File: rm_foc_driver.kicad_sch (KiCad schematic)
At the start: 88 parts, among them J1 SWD, J2 TMC4671, J3 UART, J4 TMC4671, J5 Conn_01x03, J6 Conn_01x02, J8 Conn_01x03, Q1 CSD18540Q5B, Q2 CSD18540Q5B, Q3 CSD18540Q5B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

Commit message: version 1.0.0-beta
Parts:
- removed C11, C9: 22pF, Capacitor_SMD:C_0603_1608Metric, symbol Device:C
- removed C34, C35, C36, C37: 100nF, Capacitor_SMD:C_0603_1608Metric, symbol Device:C
- removed C6: 4.7uF, Capacitor_SMD:C_0603_1608Metric, symbol Device:C
- removed D1, D2: LED, LED_SMD:LED_0603_1608Metric, symbol Device:LED
- removed J3: UART, Connector_PinHeader_2.54mm:PinHeader_1x04_P2.54mm_Horizontal, symbol Connector_Generic:Conn_01x04
- removed J4: TMC4671, Connector_PinHeader_2.54mm:PinHeader_1x04_P2.54mm_Vertical, symbol Connector_Generic:Conn_01x04
- removed J5: Conn_01x03, Connector_PinSocket_2.54mm:PinSocket_1x03_P2.54mm_Vertical, symbol Connector_Generic:Conn_01x03
- removed U3: STM32F401CCUx, Package_DFN_QFN:QFN-48-1EP_7x7mm_P0.5mm_EP5.6x5.6mm, symbol MCU_ST_STM32F4:STM32F401CCUx
- removed Y1: Crystal_GND24, Crystal:Crystal_SMD_3225-4Pin_3.2x2.5mm, symbol Device:Crystal_GND24
- added J3: Conn_01x03, Connector_PinHeader_2.54mm:PinHeader_1x03_P2.54mm_Vertical, symbol Connector_Generic:Conn_01x03
- added R21, R22: 10k, Resistor_SMD:R_0603_1608Metric, symbol Device:R
- added U3: ADS1115IDGS, Package_SO:TSSOP-10_3x3mm_P0.5mm, symbol Analog_ADC:ADS1115IDGS
- C4: value 100nF -> 1uF
- J1: value SWD -> TMC4671; footprint Connector_PinHeader_2.54mm:PinHeader_1x04_P2.54mm_Horizontal -> Connector_PinHeader_2.54mm:PinHeader_1x04_P2.54mm_Vertical
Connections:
- net CS1 is gone; now on net +5V: U7.8 (Z)
- net SWCLK is gone; now on net SDA1: J1.3 (Pin_3)
- net +3.3V: no longer J1.1 (Pin_1), R1.2, R4.1, R5.1
- net +5V: now also C4.1, R1.1, R3.1, R4.1, R21.1, R22.1, U3.8 (VDD)
- net GND: now also R5.1, J3.3 (Pin_3), U3.3 (GND); no longer R3.2
- net SO1: now also U3.4 (AIN0)
- net SO2: now also U3.5 (AIN1)
- net at R5.2: now also U3.1 (ADDR)
- net SDA1: now reaches R4.2
- net SDA1: now also U3.9 (SDA)
- net MISO renamed SDA2
- net SDA2: now also J3.2 (Pin_2), R21.2
- net SCLK renamed SCL2
- net SCL2: now also J3.1 (Pin_1), R22.2
- net SWDIO renamed SCL1
- net SCL1: now also R3.2, U3.10 (SCL)
- new net RDY: J1.1 (Pin_1), R1.2, U3.2 (ALERT/RDY)
- no-connect marks 37 -> 17
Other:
- note added: "ADC MODULE"
- note removed: "MCU"

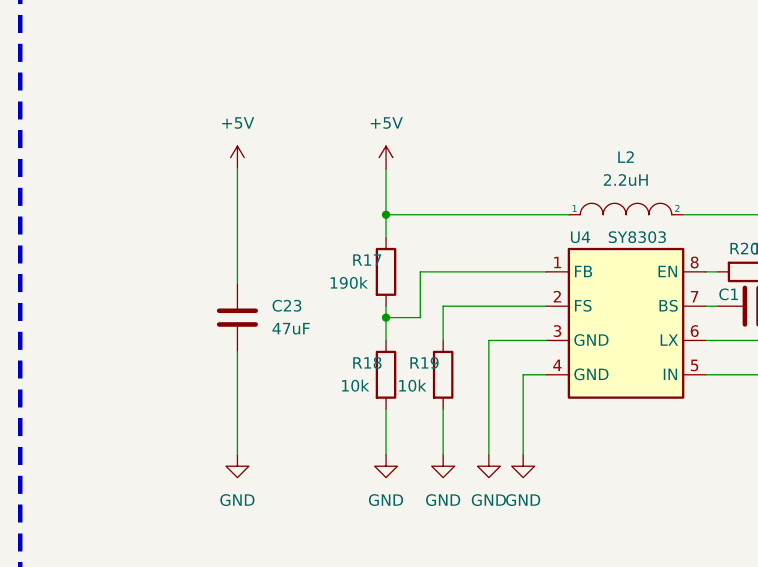
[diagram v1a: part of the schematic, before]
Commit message: version 1.0.0-beta.Round-angle PCB-layout
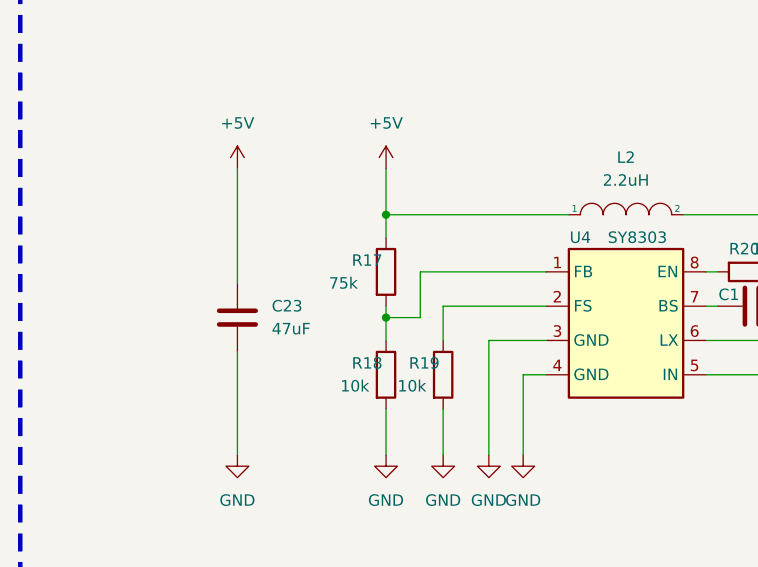
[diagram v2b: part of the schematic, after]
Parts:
- R17: value 190k -> 75k
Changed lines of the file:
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@@
       (effects (font (size 1.27 1.27)) (justify left))
     )
-    (property "Value" "190k" (id 1) (at 54.61 133.35 0)
+    (property "Value" "75k" (id 1) (at 54.61 133.35 0)
       (effects (font (size 1.27 1.27)) (justify left))
     )
@@
     )
     (path "/b9698de5-21a4-4bea-8f42-d108c2a3a546"
-      (reference "R17") (unit 1) (value "190k") (footprint "Resistor_SMD:R_0603_1608Metric")
+      (reference "R17") (unit 1) (value "75k") (footprint "Resistor_SMD:R_0603_1608Metric")
     )
     (path "/70b14ddb-ab68-49ec-87c1-af3e97ca389f"
